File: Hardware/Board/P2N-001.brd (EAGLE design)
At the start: 72 x 72 mm, 36 parts, among them IC1 4053N, IC2 LTC485N, IC3 74LS07N, IC4 LTC485N, K1 G5V1, T1 2SC1815

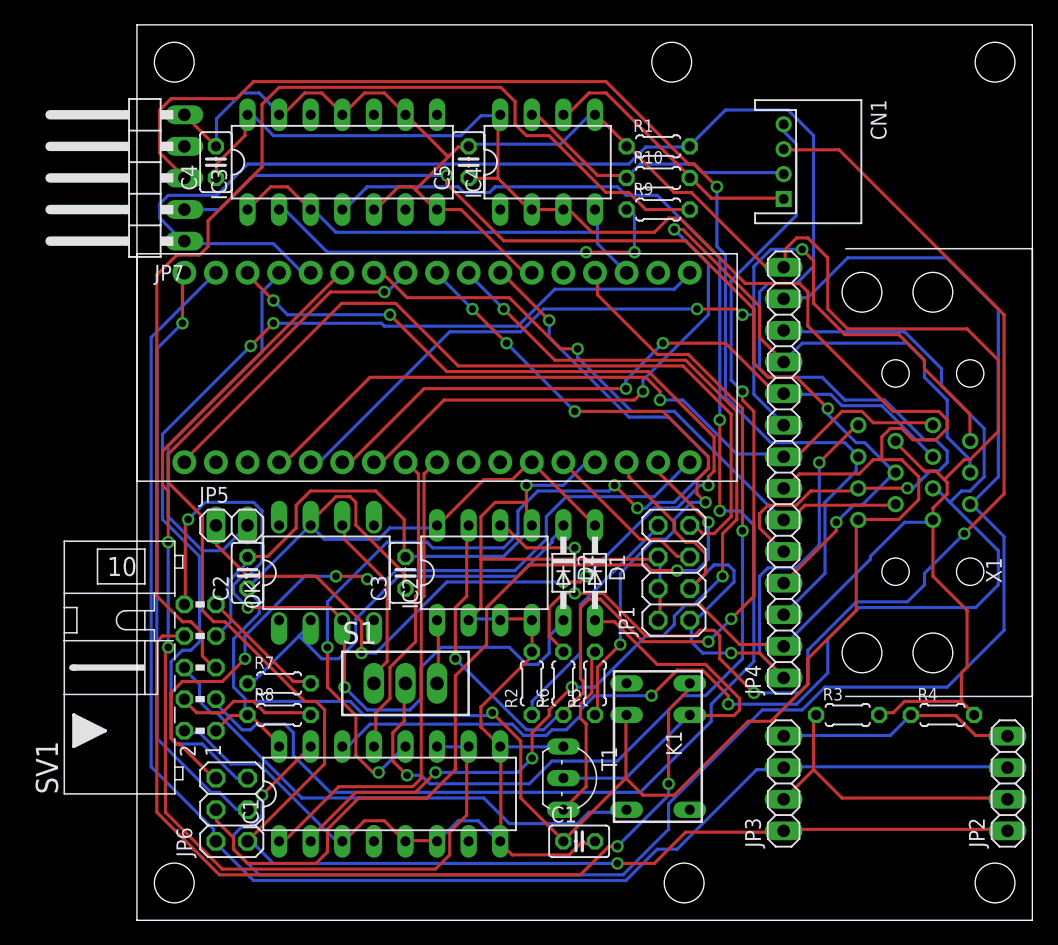
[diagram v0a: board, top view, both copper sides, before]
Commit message: Removed LED jumper.
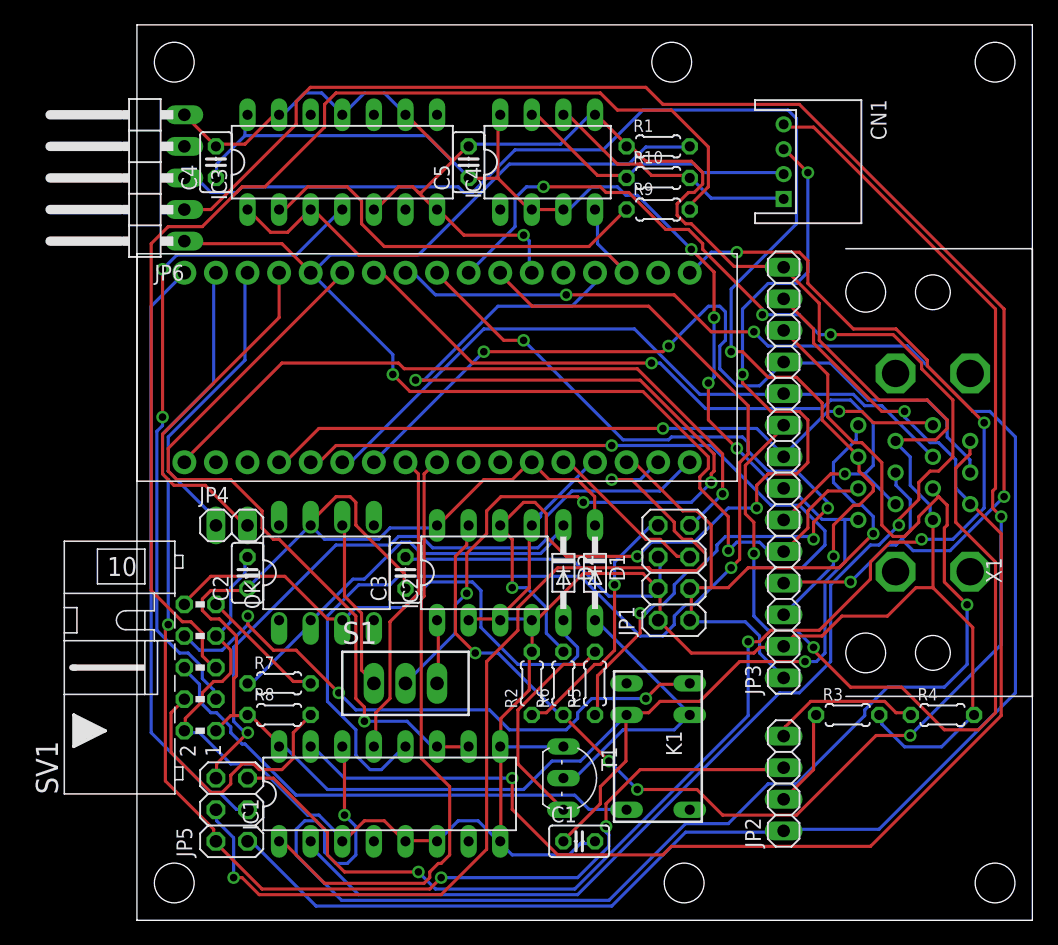
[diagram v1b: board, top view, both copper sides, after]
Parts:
- removed JP7: (no value), pinhead:1X05/90
- JP3: device pinhead:1X04 -> pinhead:1X14
- JP4: device pinhead:1X14 -> pinhead:1X02
- JP5: device pinhead:1X02 -> pinhead:2X03
- JP6: device pinhead:2X03 -> pinhead:1X05/90
- moved JP6 51.4 mm to (0.00, 59.7)
- moved JP4 44.6 mm to (7.62, 31.8), turned to 0 degrees
- moved JP3 25.0 mm to (52.0, 36.0)
- moved JP5 22.9 mm to (7.62, 8.89), turned to 90 degrees
- moved JP2 18.0 mm to (52.0, 11.0)
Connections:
- net ANLG0: now also JP3.8; no longer JP4.8
- net ANLG1: now also JP3.9; no longer JP4.9
- net ANLG2: now also JP3.10; no longer JP4.10
- net ANLG3: now also JP3.11; no longer JP4.11
- net CD: now also JP3.6; no longer JP4.6
- net GND: now also JP3.14, JP3.2, JP6.5; no longer JP4.14, JP4.2, JP7.5
- net GPIO0: now also JP5.1; no longer JP3.1, JP6.1
- net GPIO1: now also JP5.2; no longer JP3.3, JP6.2
- net GPIO2: now also JP5.3; no longer JP6.3
- net MISO: now also JP5.4; no longer JP6.4
- net MOSI: now also JP5.5; no longer JP6.5
- net N$17: no longer JP3.2
- net N$18: no longer JP3.4
- net N$28: now also JP3.12; no longer JP4.12
- net N$29: now also JP3.13; no longer JP4.13
- net PD: now also JP3.5, JP6.1; no longer JP4.5, JP7.1
- net SCLK: now also JP5.6; no longer JP6.6
- net SX: now also JP4.1; no longer JP5.1
- net SY: now also JP4.2; no longer JP5.2
- net USBD+: now also JP3.3, JP6.3; no longer JP4.3, JP7.3
- net USBD-: now also JP3.4, JP6.2; no longer JP4.4, JP7.2
- net VCC: now also JP3.7; no longer JP4.7
- net VDD: now also JP3.1; no longer JP4.1
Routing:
- net SX: track 98.9 -> 24.6 mm, vias 6 -> 0
- net RAWTX: track 121.7 -> 53.6 mm
- net SCL: track 84.0 -> 128.6 mm, vias 5 -> 4
- net MOSI: track 82.5 -> 119.2 mm, vias 2 -> 5
- net USBD-: track 84.5 -> 121.0 mm, vias 3 -> 2
- net ANLG1: track 82.7 -> 117.0 mm
- net VCC: track 257.7 -> 228.4 mm, vias 1 -> 5
- net SEL: track 86.9 -> 60.5 mm, vias 2 -> 1
- net PD: track 133.0 -> 107.7 mm, vias 1 -> 2
- net RX-: track 90.6 -> 115.4 mm, vias 4 -> 5
- net N$29: track 131.7 -> 107.5 mm, vias 1 -> 2
- net RX+: track 102.7 -> 78.6 mm, vias 4 -> 5
- net CB: track 71.7 -> 48.6 mm, vias 2 -> 3
- net N$28: track 101.3 -> 124.1 mm
- net RXK: track 61.5 -> 43.5 mm, vias 3 -> 0
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
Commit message: Cleaned up schematic and board design of P2N.
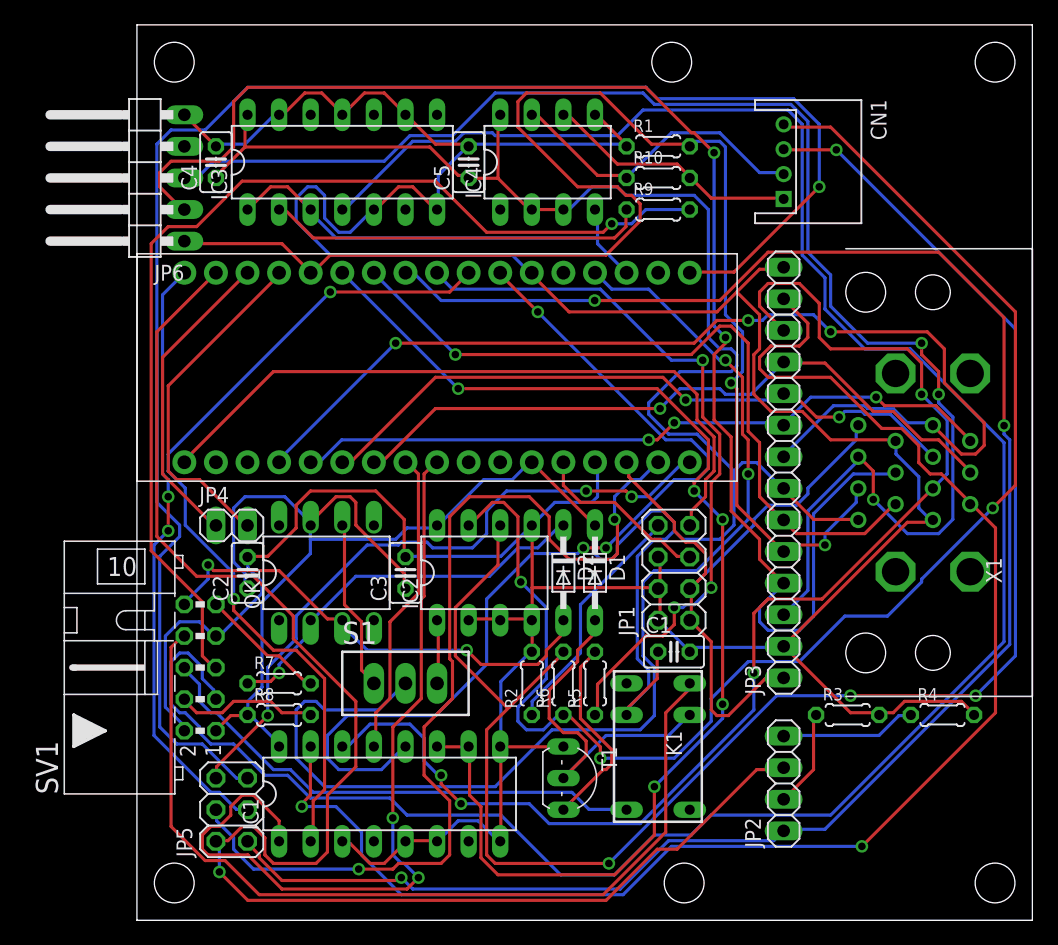
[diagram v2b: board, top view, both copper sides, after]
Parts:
- moved C1 17.0 mm to (43.2, 21.6)
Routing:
- net RAWTX: track 53.6 -> 181.9 mm, vias 2 -> 0
- net SCL: track 128.6 -> 68.2 mm, vias 4 -> 2
- net ANLG1: track 117.0 -> 56.9 mm
- net RX+: track 78.6 -> 137.5 mm, vias 5 -> 4
- net SEL: track 60.5 -> 98.2 mm, vias 1 -> 5
- net ANLG0: track 56.8 -> 88.5 mm, vias 2 -> 3
- net CB: track 48.6 -> 72.8 mm, vias 3 -> 0
- net N$28: track 124.1 -> 101.6 mm, vias 2 -> 4
- net GPIO1: track 103.2 -> 124.0 mm, vias 3 -> 1
- net SDA: track 93.8 -> 75.7 mm, vias 1 -> 3
- net ANLG5: track 49.5 -> 66.5 mm, vias 0 -> 2
- net USBD+: track 105.1 -> 120.6 mm, vias 2 -> 3
- net N$29: track 107.5 -> 120.3 mm
- net MOSI: track 119.2 -> 131.7 mm, vias 5 -> 1
- net RX: track 83.3 -> 94.9 mm, vias 4 -> 2
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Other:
- board text added: "PINEAPPLE II NITROGEN 14 REVISION 1.0.0 (2015)"
- board text removed: "PINEAPPLE II NITROGEN REVISION 1.0.0 (2015)"

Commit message: Added Reset SW.
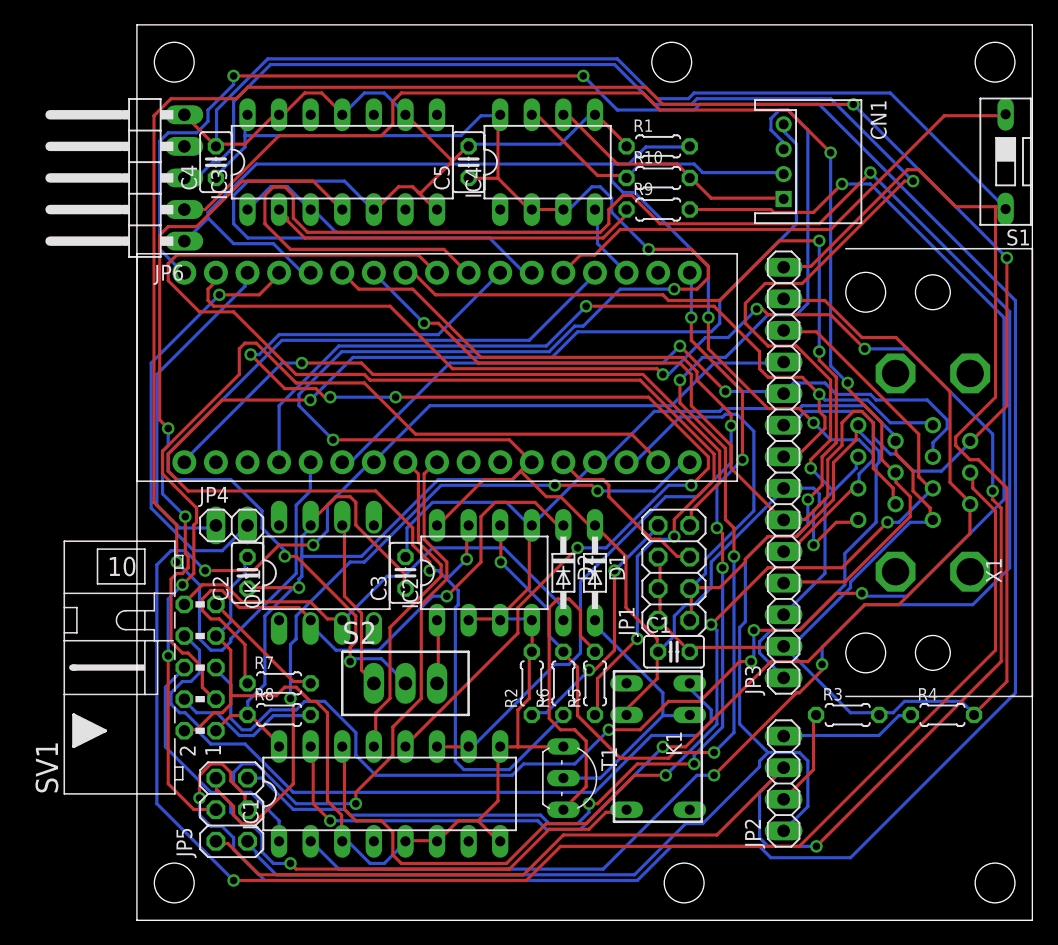
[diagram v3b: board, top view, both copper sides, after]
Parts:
- added S2: TL36PO, switch:TL3XPO
- S1: value TL36PO -> (none); device switch:TL3XPO -> switch-dil:DS-01
- moved S1 63.9 mm to (69.8, 61.0), turned to 180 degrees
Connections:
- new net N$1: MC1.P$22, S1.1
- net GND: now also S1.2
- net MIDIRX: now also S2.1; no longer S1.1
- net RX: now also S2.2; no longer S1.2
- net XMIDIRX: now also S2.3; no longer S1.3
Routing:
- net GPIO2: track 48.6 -> 208.1 mm, vias 2 -> 3
- net RAWTX: track 181.9 -> 58.7 mm, vias 0 -> 2
- net ANLG1: track 56.9 -> 174.3 mm
- net ANLG3: track 55.4 -> 172.0 mm, vias 1 -> 3
- net GND: track 320.2 -> 435.6 mm
- net SCL: track 68.2 -> 181.1 mm, vias 2 -> 3
- net GPIO1: track 124.0 -> 175.7 mm, vias 1 -> 5
- net MOSI: track 131.7 -> 83.1 mm, vias 1 -> 6
- net RETURN: track 84.2 -> 127.7 mm, vias 1 -> 5
- net RX+: track 137.5 -> 96.4 mm
- net N$1: track 0.00 -> 40.9 mm
- net RELAY: track 59.2 -> 99.3 mm, vias 3 -> 2
- net VDD: track 51.8 -> 78.5 mm
- net N$29: track 120.3 -> 96.9 mm
- net VCC: track 222.4 -> 245.8 mm, vias 0 -> 5
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
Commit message: Added MIDI THRU function.
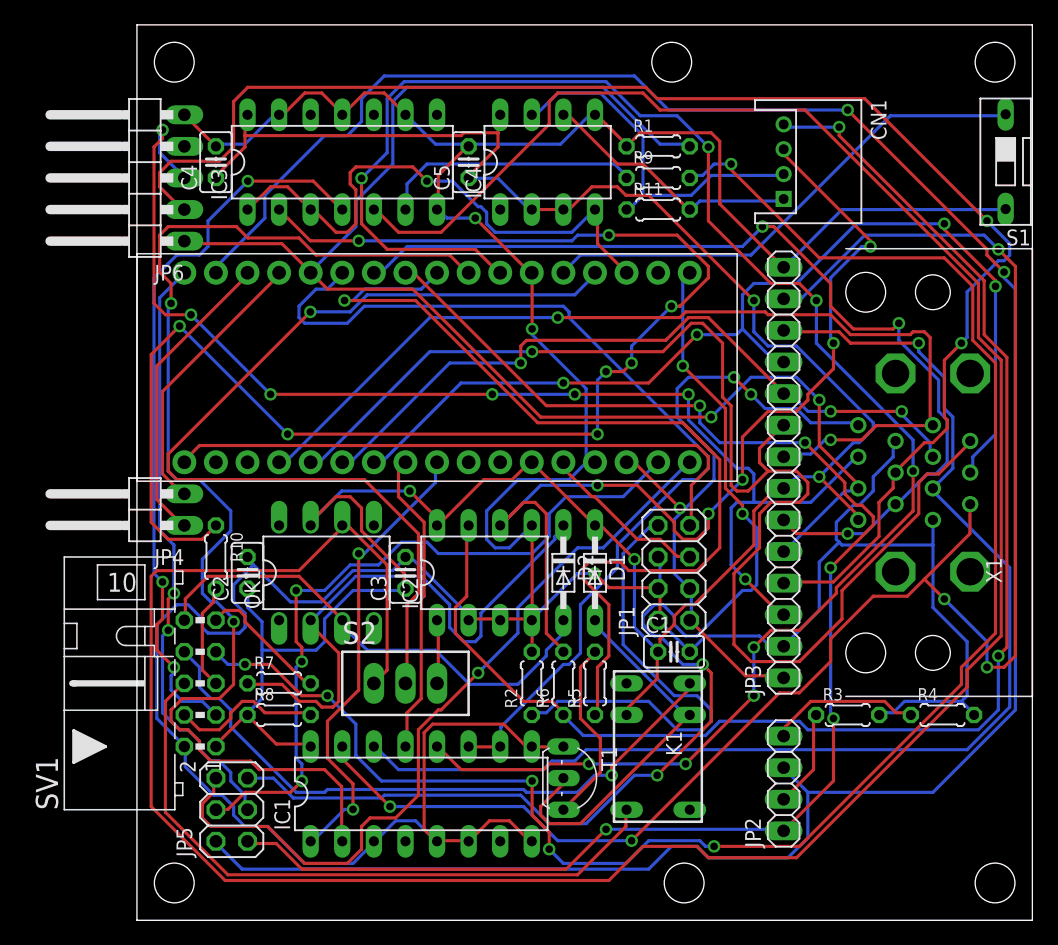
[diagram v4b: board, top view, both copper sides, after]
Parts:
- added R11: 120, resistor:0204/5
- JP4: device pinhead:1X02 -> pinhead:1X02/90
- R10: value 120 -> 220
- moved R10 46.8 mm to (6.35, 29.2), turned to 270 degrees
- moved JP4 7.73 mm to (0.00, 33.0), turned to 90 degrees
- moved IC1 2.54 mm to (22.9, 10.2)
- moved R9 2.54 mm to (41.9, 59.7)
- moved SV1 1.27 mm to (5.08, 19.1)
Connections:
- new net N$3: IC3.6, R9.1
- new net N$4: R9.2, SV1.7
- net GND: no longer IC3.5, SV1.7
- net MIDIRX: now also IC3.5
- net N$2: now also R10.1; no longer R9.1
- net RETURN: now also R10.2; no longer R9.2
- net TX+: now also R11.2; no longer R10.2
- net TX-: now also R11.1; no longer R10.1
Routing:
- net MIDIRX: track 13.7 -> 221.6 mm
- net GPIO2: track 208.1 -> 48.6 mm, vias 3 -> 2
- net N$4: track 0.00 -> 138.7 mm, vias 0 -> 6
- net RETURN: track 127.7 -> 8.54 mm, vias 5 -> 0
- net GND: track 435.6 -> 340.7 mm, vias 0 -> 3
- net ANLG3: track 172.0 -> 82.5 mm, vias 3 -> 4
- net N$2: track 30.2 -> 115.3 mm, vias 0 -> 8
- net SCL: track 181.1 -> 96.2 mm, vias 3 -> 2
- net ANLG1: track 174.3 -> 109.0 mm, vias 3 -> 1
- net SDA: track 98.8 -> 139.9 mm, vias 5 -> 8
- net VCC: track 245.8 -> 207.2 mm, vias 5 -> 4
- net N$29: track 96.9 -> 132.9 mm, vias 2 -> 5
- net VDD: track 78.5 -> 54.0 mm, vias 0 -> 3
- net USBD+: track 122.4 -> 98.9 mm, vias 2 -> 7
- net MISO: track 82.2 -> 58.9 mm, vias 2 -> 3
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
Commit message: Updated Hirose DX10LM1-14SE connector pattern.
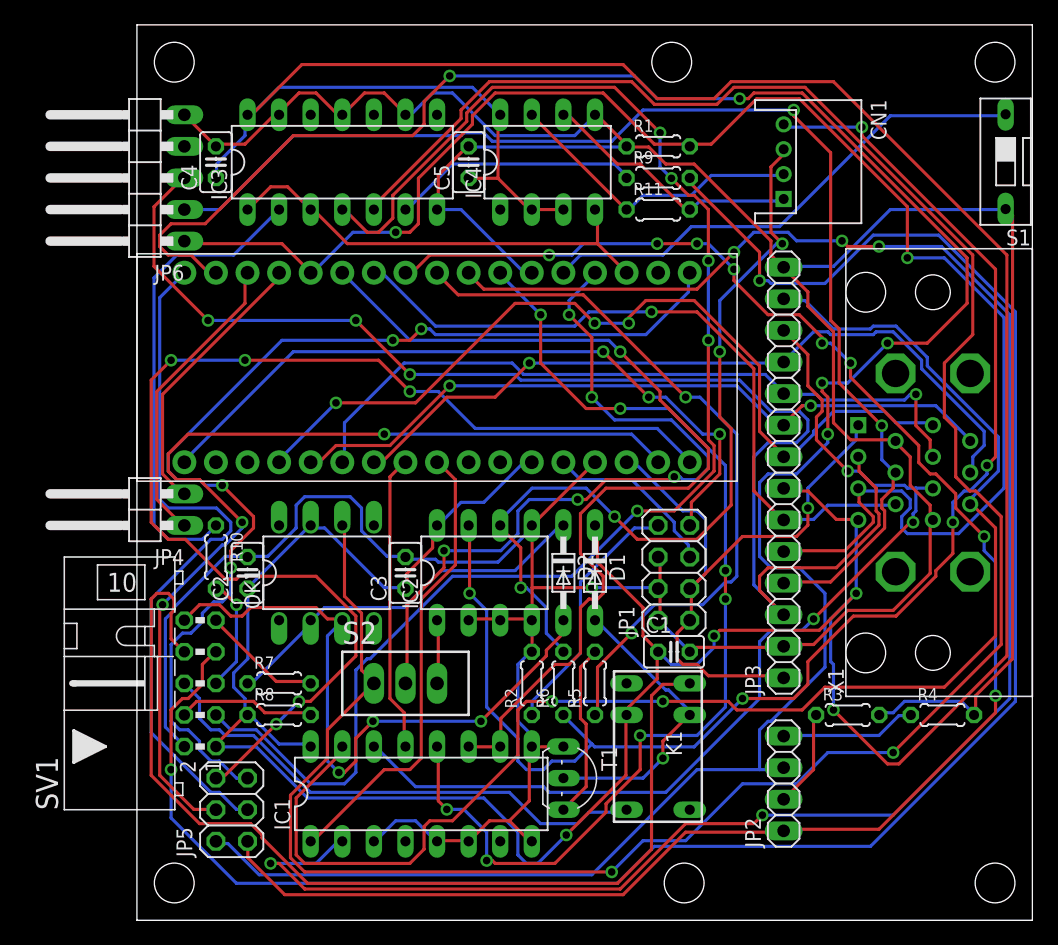
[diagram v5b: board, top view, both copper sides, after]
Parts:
- X1: value (none) -> HIROSE-DX10LM1-14SE; device con-hirose-dxlm:HIROSE-DXLM -> con-hirose-dx10lm1-14se:HIROSE-DX10LM1-14SE
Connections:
- net ANLG0: now also X1.P$8; no longer X1.8
- net ANLG1: now also X1.P$9; no longer X1.9
- net ANLG2: now also X1.P$10; no longer X1.10
- net ANLG3: now also X1.P$11; no longer X1.11
- net CD: now also X1.P$6; no longer X1.6
- net GND: now also X1.P$14, X1.P$2; no longer X1.14, X1.2
- net N$28: now also X1.P$12; no longer X1.12
- net N$29: now also X1.P$13; no longer X1.13
- net PD: now also X1.P$5; no longer X1.5
- net USBD+: now also X1.P$3; no longer X1.3
- net USBD-: now also X1.P$4; no longer X1.4
- net VCC: now also X1.P$7; no longer X1.7
- net VDD: now also X1.P$1; no longer X1.1
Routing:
- net VCC: track 207.2 -> 324.8 mm
- net N$2: track 115.3 -> 38.1 mm, vias 8 -> 0
- net RAWTX: track 59.2 -> 121.0 mm, vias 3 -> 5
- net SCL: track 96.2 -> 152.8 mm, vias 2 -> 5
- net SDA: track 139.9 -> 84.5 mm, vias 8 -> 7
- net ANLG1: track 109.0 -> 58.8 mm, vias 1 -> 2
- net SCLK: track 63.2 -> 97.1 mm, vias 1 -> 5
- net MIDIRX: track 221.6 -> 190.2 mm, vias 0 -> 2
- net CB: track 51.6 -> 82.1 mm, vias 1 -> 0
- net GPIO0: track 121.0 -> 143.5 mm, vias 5 -> 8
- net ANLG3: track 82.5 -> 61.2 mm, vias 4 -> 1
- net MISO: track 58.9 -> 79.0 mm
- net USBD-: track 120.4 -> 100.4 mm
- net CD: track 77.3 -> 57.4 mm, vias 3 -> 1
- net N$4: track 138.7 -> 158.1 mm, vias 6 -> 2
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
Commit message: Changed R value of main LED (from 220 to 150 ohm).
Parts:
- R2: value 220 -> 150
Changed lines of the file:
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@@
 <element name="R7" library="resistor" package="0204/5" value="220" x="11.43" y="19.05"/>
 <element name="MC1" library="adafruit" package="ARDUINOMICRO" value="ARDUINOMICRO" x="24.13" y="44.45"/>
-<element name="R2" library="resistor" package="0204/5" value="220" x="31.75" y="19.05" rot="R90"/>
+<element name="R2" library="resistor" package="0204/5" value="150" x="31.75" y="19.05" rot="R90"/>
 <element name="SV1" library="con-ml" package="ML10L" value="" x="5.08" y="19.05" rot="R90">
 <attribute name="OC_NEWARK" value="unknown" x="5.08" y="19.05" size="1.778" layer="27" rot="R90" display="off"/>
